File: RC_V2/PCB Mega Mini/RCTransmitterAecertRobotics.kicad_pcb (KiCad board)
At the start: 2 copper layers, 124.5 x 86.4 mm, 40 parts, among them K1 KCD1 Power Switch

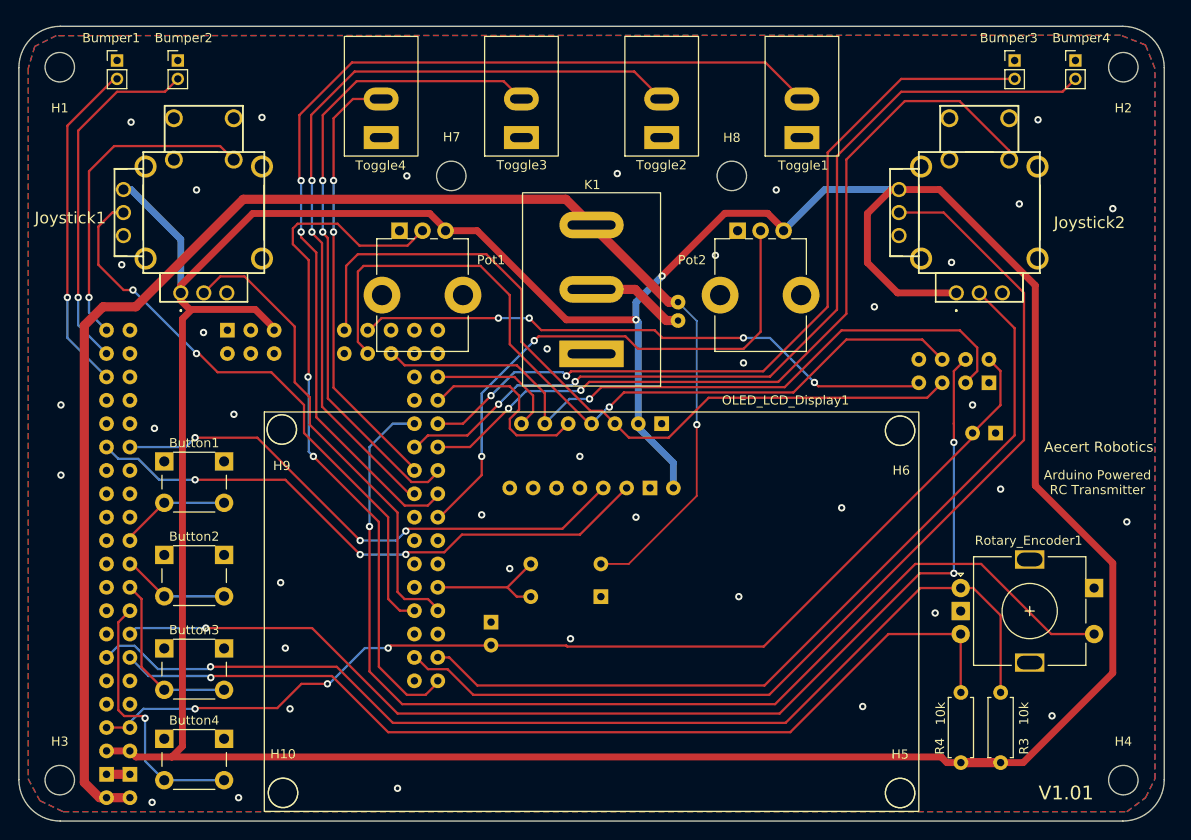
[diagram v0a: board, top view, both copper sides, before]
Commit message: Updated PCB, Made screen spacer and backplate
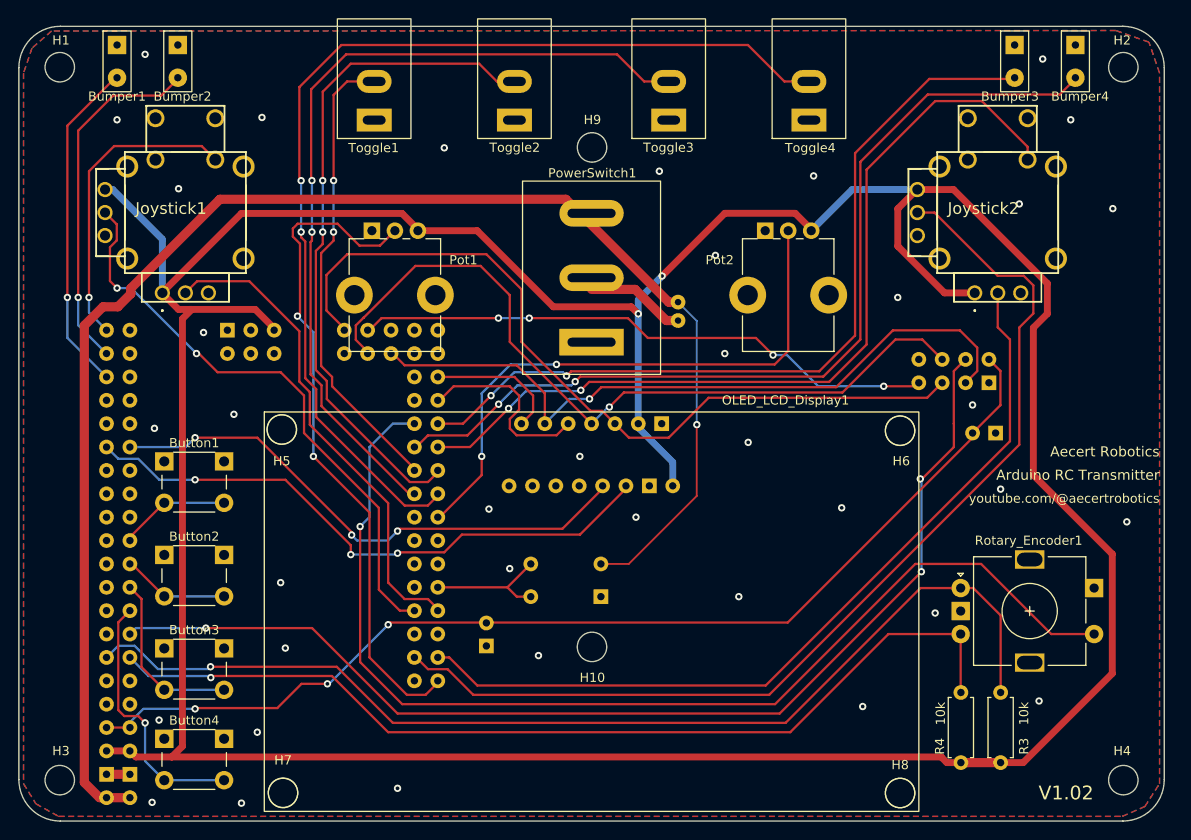
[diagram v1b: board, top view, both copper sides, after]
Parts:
- Bumper1, Bumper2, Bumper3, Bumper4: footprint Connector_PinHeader_2.00mm:PinHeader_1x02_P2.00mm_Vertical -> AddedFootprints:Bumper Pads
- moved H10 53.4 mm to (141.0, 123.3)
- moved H9 15.6 mm to (141.0, 69.0)
- moved Bumper1 5.43 mm to (89.4, 65.0)
- moved Bumper2 5.43 mm to (96.0, 65.0)
- moved Bumper3 5.43 mm to (186.9, 65.0)
- moved Bumper4 5.43 mm to (193.5, 65.0)
- moved Pot1 3.00 mm to (117.1, 78.1)
- moved Pot2 3.00 mm to (159.8, 78.1)
- moved C2 2.46 mm to (129.5, 120.7), turned to -90 degrees
- moved Toggle1 2.05 mm to (117.3, 68.1)
- moved Toggle2 2.05 mm to (132.6, 68.1)
- moved Toggle3 2.05 mm to (149.4, 68.1)
- moved Toggle4 2.05 mm to (164.6, 68.1)
- moved Joystick1 2.00 mm to (94.3, 84.8)
- moved Joystick2 2.00 mm to (182.6, 84.8)
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- renumbered H8 to H10, H9 to H5, H10 to H7, H5 to H8, H7 to H9, K1 to PowerSwitch1, Toggle4 to Toggle1, Toggle3 to Toggle2, Toggle2 to Toggle3, Toggle1 to Toggle4
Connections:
- Arduino_Mega_Pro1 pad 32: /Toggle A -> /Toggle D
- Arduino_Mega_Pro1 pad 33: /Toggle B -> /Toggle C
- Arduino_Mega_Pro1 pad 34: /Toggle C -> /Toggle B
- Arduino_Mega_Pro1 pad 35: /Toggle D -> /Toggle A
- Toggle1 pad 2: /Toggle D -> /Toggle A
- Toggle2 pad 2: /Toggle C -> /Toggle B
- Toggle3 pad 2: /Toggle B -> /Toggle C
- Toggle4 pad 2: /Toggle A -> /Toggle D
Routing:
- net /Toggle D: track 48.0 -> 113.4 mm
- net /Toggle A: track 110.1 -> 50.7 mm
- net /Toggle C: track 71.4 -> 90.9 mm
- net /Toggle B: track 87.6 -> 73.6 mm
- net /Joy Right Button: track 90.5 -> 94.0 mm
- net /MOSI: track 88.1 -> 84.8 mm
- net /Pot Right: track 60.5 -> 63.8 mm
- net /Pot Left: track 76.0 -> 73.2 mm
- net /SCK: track 86.4 -> 88.8 mm
- net /Joy Left Button: track 35.5 -> 33.5 mm
- net /NRF CSN: track 123.7 -> 121.8 mm
- net /Right Bumper A: track 88.2 -> 89.9 mm
- net /Joy Left X: track 51.8 -> 53.3 mm
- net /Right Bumper B: track 98.0 -> 99.5 mm
- net /5v: track 391.6 -> 393.0 mm
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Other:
- board text added: "Arduino RC Transmitter"
- board text added: "V1.02"
- board text added: "youtube.com/@aecertrobotics"
- board text removed: "Arduino Powered RC Transmitter"
- board text removed: "V1.01"

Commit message: added + and - to jst connector
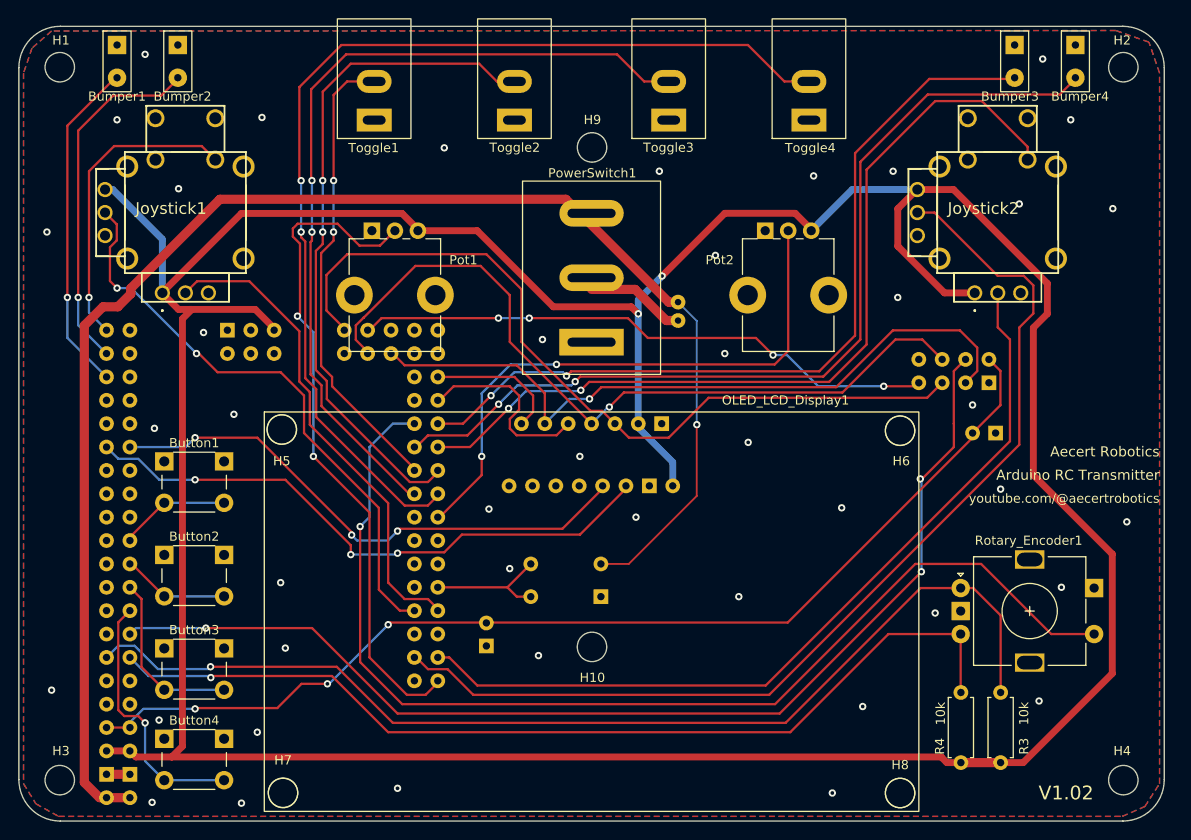
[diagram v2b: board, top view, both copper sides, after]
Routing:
- net GND: vias 38 -> 44
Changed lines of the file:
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@@
     (property "ki_keywords" "connector")
     (attr through_hole)
-    (fp_text reference "JST_Connector1" (at -3.913441 2.076364 unlocked) (layer "B.SilkS")
+    (fp_text reference "JST_Connector1" (at -7.551317 3.60201 unlocked) (layer "B.SilkS")
         (effects (font (size 1 1) (thickness 0.1)) (justify mirror))
     )
     (fp_text value "1.27mm_JST_Connector_1" (at 0 -1 unlocked) (layer "B.Fab")
         (effects (font (size 1 1) (thickness 0.15)) (justify mirror))
+    )
+    (fp_text user "-" (at 1.654229 3.766833 unlocked) (layer "B.SilkS")
+        (effects (font (size 1 1) (thickness 0.1)) (justify left bottom mirror))
+    )
+    (fp_text user "+" (at 1.654229 5.873417 unlocked) (layer "B.SilkS")
+        (effects (font (size 1 1) (thickness 0.1)) (justify left bottom mirror))
     )
     (fp_text user "${REFERENCE}" (at 0 -2.5 unlocked) (layer "B.Fab")
@@
   (segment (start 184.912 100.076) (end 184.912 100.262082) (width 0.25) (layer "F.Cu") (net 2))
   (segment (start 88.265 137.16) (end 90.805 137.16) (width 1) (layer "F.Cu") (net 2))
+  (via (at 81.788 78.232) (size 0.8) (drill 0.4) (layers "F.Cu" "B.Cu") (free) (net 2))
   (via (at 154.432 80.772) (size 0.8) (drill 0.4) (layers "F.Cu" "B.Cu") (free) (net 2))
   (via (at 155.448 91.44) (size 0.8) (drill 0.4) (layers "F.Cu" "B.Cu") (free) (net 2))
@@
   (via (at 139.7 102.616) (size 0.8) (drill 0.4) (layers "F.Cu" "B.Cu") (free) (net 2))
   (via (at 156.972 117.856) (size 0.8) (drill 0.4) (layers "F.Cu" "B.Cu") (free) (net 2))
+  (via (at 167.132 139.192) (size 0.8) (drill 0.4) (layers "F.Cu" "B.Cu") (free) (net 2))
   (via (at 102.929041 140.295973) (size 0.8) (drill 0.4) (layers "F.Cu" "B.Cu") (free) (net 2))
+  (via (at 173.736 71.628) (size 0.8) (drill 0.4) (layers "F.Cu" "B.Cu") (free) (net 2))
   (via (at 129.820556 108.337148) (size 0.8) (drill 0.4) (layers "F.Cu" "B.Cu") (free) (net 2))
   (via (at 182.372 97.028) (size 0.8) (drill 0.4) (layers "F.Cu" "B.Cu") (free) (net 2))
@@
   (via (at 132.08 114.808) (size 0.8) (drill 0.4) (layers "F.Cu" "B.Cu") (free) (net 2))
   (via (at 178.308 119.634) (size 0.8) (drill 0.4) (layers "F.Cu" "B.Cu") (free) (net 2))
+  (via (at 192.024 116.84) (size 0.8) (drill 0.4) (layers "F.Cu" "B.Cu") (free) (net 2))
   (via (at 148.336 71.628) (size 0.8) (drill 0.4) (layers "F.Cu" "B.Cu") (free) (net 2))
   (via (at 107.696 123.444) (size 0.8) (drill 0.4) (layers "F.Cu" "B.Cu") (free) (net 2))
+  (via (at 135.636 89.916) (size 0.8) (drill 0.4) (layers "F.Cu" "B.Cu") (free) (net 2))
   (via (at 96.092572 73.528443) (size 0.8) (drill 0.4) (layers "F.Cu" "B.Cu") (free) (net 2))
   (via (at 93.218 140.208) (size 0.8) (drill 0.4) (layers "F.Cu" "B.Cu") (free) (net 2))
@@
   (via (at 189.59418 129.195269) (size 0.8) (drill 0.4) (layers "F.Cu" "B.Cu") (free) (net 2))
   (via (at 197.612 75.692) (size 0.8) (drill 0.4) (layers "F.Cu" "B.Cu") (free) (net 2))
+  (via (at 82.296 128.016) (size 0.8) (drill 0.4) (layers "F.Cu" "B.Cu") (free) (net 2))
   (via (at 124.968 69.088) (size 0.8) (drill 0.4) (layers "F.Cu" "B.Cu") (free) (net 2))
   (via (at 170.434 129.794) (size 0.8) (drill 0.4) (layers "F.Cu" "B.Cu") (free) (net 2))
